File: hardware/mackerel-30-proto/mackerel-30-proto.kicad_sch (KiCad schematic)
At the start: 37 parts, among them J1 Conn_01x02, J2 Conn_01x02, J3 Conn_02x05_Odd_Even, U1 MC68030RC, U2 EPM7128, X1 CXO_DIP14

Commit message: Rough routing of data bus to FPU and RAM
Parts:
- C1, C10, C2, C3, C4, C5, C6, C7, C8, C9: footprint Capacitor_THT:C_Disc_D4.3mm_W1.9mm_P5.00mm -> Capacitor_SMD:C_1206_3216Metric_Pad1.33x1.80mm_HandSolder
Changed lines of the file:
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@@
 			)
 		)
-		(property "Footprint" "Capacitor_THT:C_Disc_D4.3mm_W1.9mm_P5.00mm"
+		(property "Footprint" "Capacitor_SMD:C_1206_3216Metric_Pad1.33x1.80mm_HandSolder"
 			(at 24.13 70.1548 0)
 			(effects
@@
 			)
 		)
-		(property "Footprint" "Capacitor_THT:C_Disc_D4.3mm_W1.9mm_P5.00mm"
+		(property "Footprint" "Capacitor_SMD:C_1206_3216Metric_Pad1.33x1.80mm_HandSolder"
 			(at 24.13 65.0748 0)
 			(effects
@@
 			)
 		)
-		(property "Footprint" "Capacitor_THT:C_Disc_D4.3mm_W1.9mm_P5.00mm"
+		(property "Footprint" "Capacitor_SMD:C_1206_3216Metric_Pad1.33x1.80mm_HandSolder"
 			(at 24.13 29.5148 0)
 			(effects
@@
 			)
 		)
-		(property "Footprint" "Capacitor_THT:C_Disc_D4.3mm_W1.9mm_P5.00mm"
+		(property "Footprint" "Capacitor_SMD:C_1206_3216Metric_Pad1.33x1.80mm_HandSolder"
 			(at 24.13 59.9948 0)
 			(effects
@@
 			)
 		)
-		(property "Footprint" "Capacitor_THT:C_Disc_D4.3mm_W1.9mm_P5.00mm"
+		(property "Footprint" "Capacitor_SMD:C_1206_3216Metric_Pad1.33x1.80mm_HandSolder"
 			(at 24.13 44.7548 0)
 			(effects
@@
 			)
 		)
-		(property "Footprint" "Capacitor_THT:C_Disc_D4.3mm_W1.9mm_P5.00mm"
+		(property "Footprint" "Capacitor_SMD:C_1206_3216Metric_Pad1.33x1.80mm_HandSolder"
 			(at 24.13 34.5948 0)
 			(effects
@@
 			)
 		)
-		(property "Footprint" "Capacitor_THT:C_Disc_D4.3mm_W1.9mm_P5.00mm"
+		(property "Footprint" "Capacitor_SMD:C_1206_3216Metric_Pad1.33x1.80mm_HandSolder"
 			(at 24.13 39.6748 0)
 			(effects
@@
 			)
 		)
-		(property "Footprint" "Capacitor_THT:C_Disc_D4.3mm_W1.9mm_P5.00mm"
+		(property "Footprint" "Capacitor_SMD:C_1206_3216Metric_Pad1.33x1.80mm_HandSolder"
 			(at 24.13 24.4348 0)
 			(effects
@@
 			)
 		)
-		(property "Footprint" "Capacitor_THT:C_Disc_D4.3mm_W1.9mm_P5.00mm"
+		(property "Footprint" "Capacitor_SMD:C_1206_3216Metric_Pad1.33x1.80mm_HandSolder"
 			(at 24.13 54.9148 0)
 			(effects
@@
 			)
 		)
-		(property "Footprint" "Capacitor_THT:C_Disc_D4.3mm_W1.9mm_P5.00mm"
+		(property "Footprint" "Capacitor_SMD:C_1206_3216Metric_Pad1.33x1.80mm_HandSolder"
 			(at 24.13 49.8348 0)
 			(effects

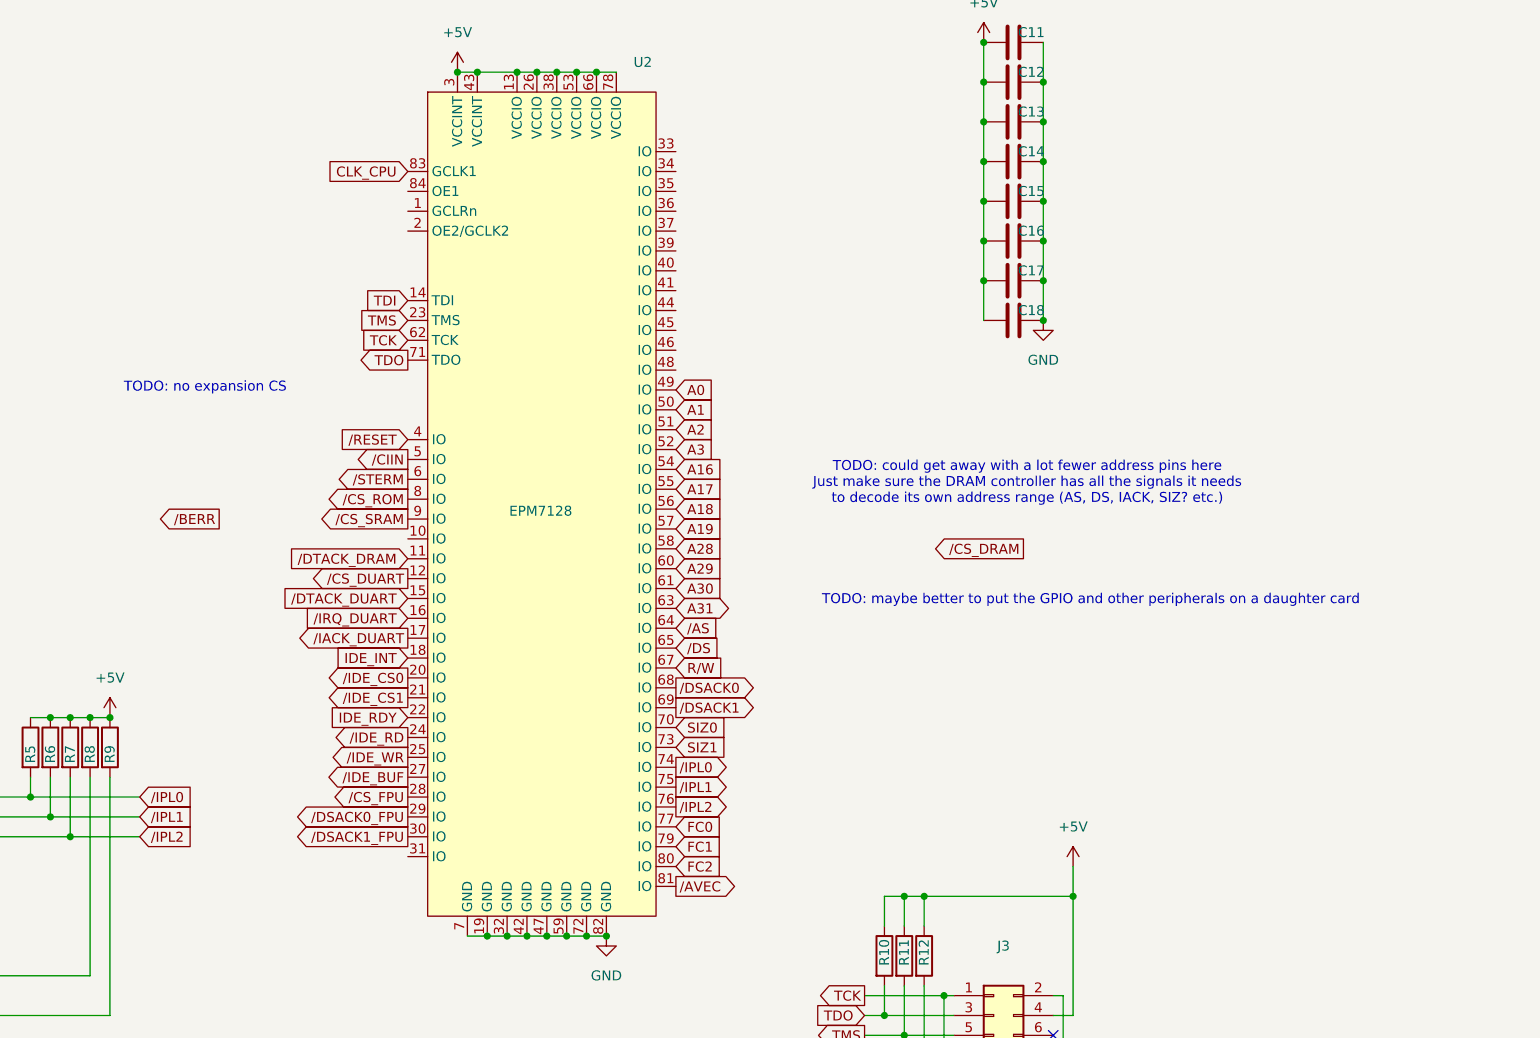
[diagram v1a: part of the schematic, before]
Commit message: Roughly routed all but expansion and reset
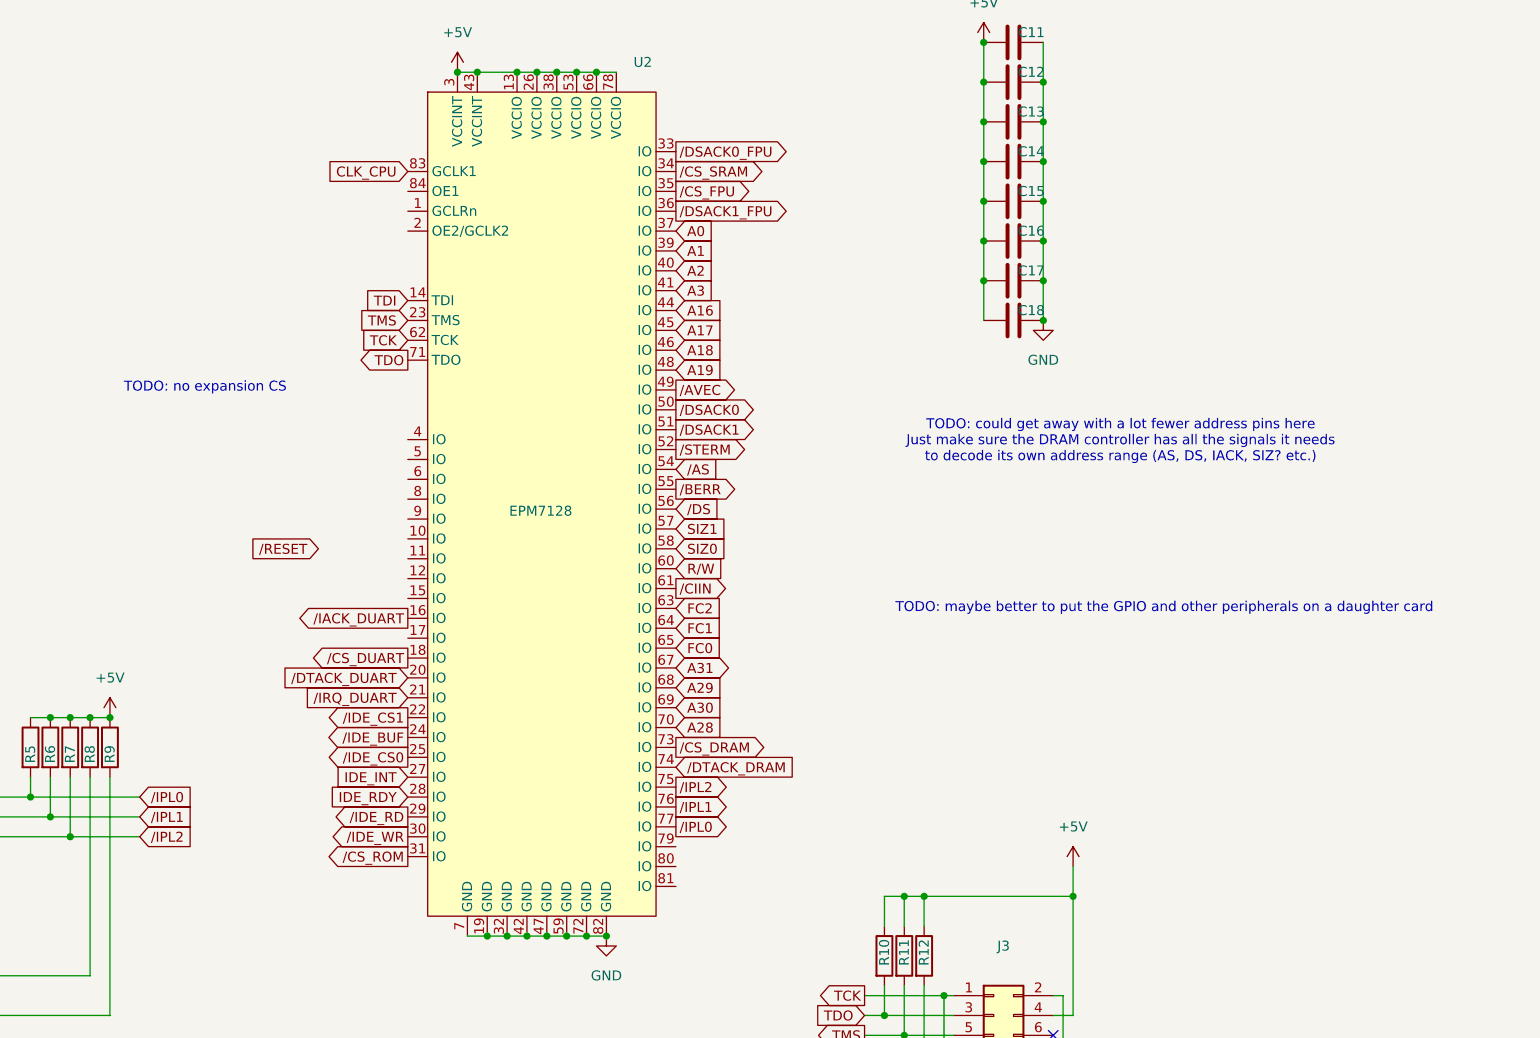
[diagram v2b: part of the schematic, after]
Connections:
- net A0: now also U2.37 (IO); no longer U2.49 (IO)
- net A1: now also U2.39 (IO); no longer U2.50 (IO)
- net A16: now also U2.44 (IO); no longer U2.54 (IO)
- net A17: now also U2.45 (IO); no longer U2.55 (IO)
- net A18: now also U2.46 (IO); no longer U2.56 (IO)
- net A19: now also U2.48 (IO); no longer U2.57 (IO)
- net A2: now also U2.40 (IO); no longer U2.51 (IO)
- net A28: now also U2.70 (IO); no longer U2.58 (IO)
- net A29: now also U2.68 (IO); no longer U2.60 (IO)
- net A3: now also U2.41 (IO); no longer U2.52 (IO)
- net A30: now also U2.69 (IO); no longer U2.61 (IO)
- net A31: now also U2.67 (IO); no longer U2.63 (IO)
- net FC0: now also U2.65 (IO); no longer U2.77 (IO)
- net FC1: now also U2.64 (IO); no longer U2.79 (IO)
- net FC2: now also U2.63 (IO); no longer U2.80 (IO)
- net IDE_INT: now also U2.27 (IO); no longer U2.18 (IO)
- net IDE_RDY: now also U2.28 (IO); no longer U2.22 (IO)
- net R/W: now also U2.60 (IO); no longer U2.67 (IO)
- net SIZ0: now also U2.58 (IO); no longer U2.70 (IO)
- net SIZ1: now also U2.57 (IO); no longer U2.73 (IO)
- net /AS: now also U2.54 (IO); no longer U2.64 (IO)
- net /AVEC: now also U2.49 (IO); no longer U2.81 (IO)
- net /BERR: now also U2.55 (IO)
- net /CIIN: now also U2.61 (IO); no longer U2.5 (IO)
- net /CS_DRAM: now also U2.73 (IO)
- net /CS_DUART: now also U2.18 (IO); no longer U2.12 (IO)
- net /CS_FPU: now also U2.35 (IO); no longer U2.28 (IO)
- net /CS_ROM: now also U2.31 (IO); no longer U2.8 (IO)
- net /CS_SRAM: now also U2.34 (IO); no longer U2.9 (IO)
- net /DS: now also U2.56 (IO); no longer U2.65 (IO)
- net /DSACK0: now also U2.50 (IO); no longer U2.68 (IO)
- net /DSACK0_FPU: now also U2.33 (IO); no longer U2.29 (IO)
- net /DSACK1: now also U2.51 (IO); no longer U2.69 (IO)
- net /DSACK1_FPU: now also U2.36 (IO); no longer U2.30 (IO)
- net /DTACK_DRAM: now also U2.74 (IO); no longer U2.11 (IO)
- net /DTACK_DUART: now also U2.20 (IO); no longer U2.15 (IO)
- net /IACK_DUART: now also U2.16 (IO); no longer U2.17 (IO)
- net /IDE_BUF: now also U2.24 (IO); no longer U2.27 (IO)
- net /IDE_CS0: now also U2.25 (IO); no longer U2.20 (IO)
- net /IDE_CS1: now also U2.22 (IO); no longer U2.21 (IO)
- net /IDE_RD: now also U2.29 (IO); no longer U2.24 (IO)
- net /IDE_WR: now also U2.30 (IO); no longer U2.25 (IO)
- net /IPL0: now also U2.77 (IO); no longer U2.74 (IO)
- net /IPL1: now also U2.76 (IO); no longer U2.75 (IO)
- net /IPL2: now also U2.75 (IO); no longer U2.76 (IO)
- net /IRQ_DUART: now also U2.21 (IO); no longer U2.16 (IO)
- net /RESET: no longer U2.4 (IO)
- net /STERM: now also U2.52 (IO); no longer U2.6 (IO)

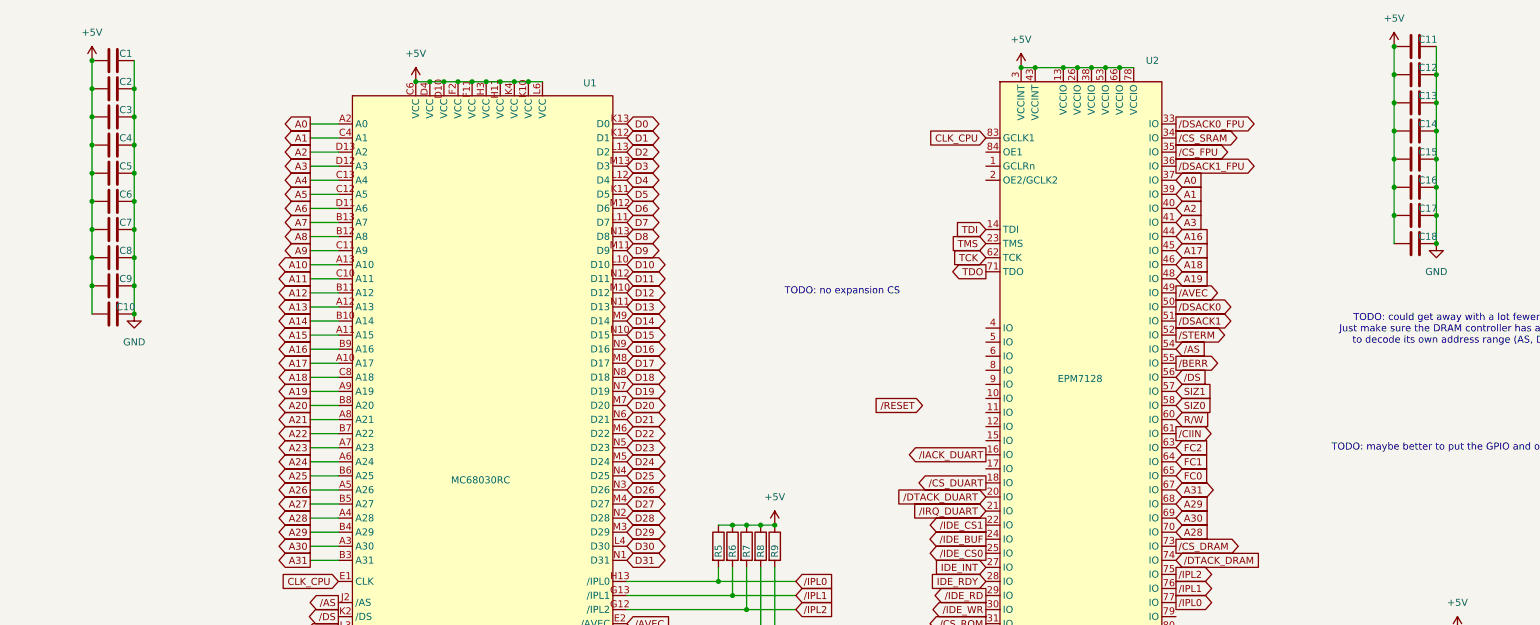
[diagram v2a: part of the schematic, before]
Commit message: Mack-30 routed except for expansion header
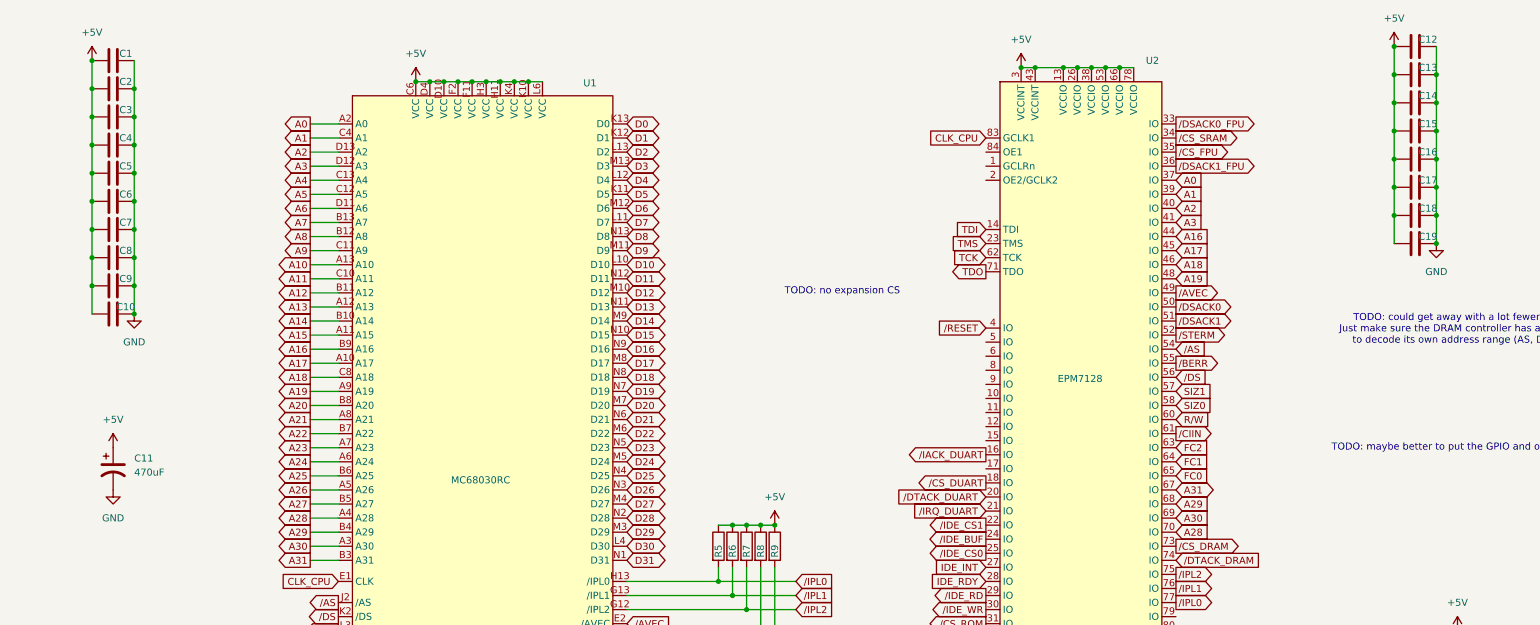
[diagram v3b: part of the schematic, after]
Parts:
- added C11: 470uF, Capacitor_THT:CP_Radial_D8.0mm_P3.50mm, symbol Device:C_Polarized_US
- renumbered C11 to C12, C12 to C13, C13 to C14, C14 to C15, C15 to C16, C16 to C17, C17 to C18, C18 to C19
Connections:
- net +5V: now also C11.1
- net GND: now also C11.2
- net /RESET: now also U2.4 (IO)
